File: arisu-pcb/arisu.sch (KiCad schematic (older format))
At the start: 40 parts, among them J1 USB_B_Micro, J10 PF6, J11 PF7, J12 VCC, J13 D+, J14 D-, J15 GND, J2 MISO, J3 VCC, J4 SCK, J5 MOSI, J6 RES, J7 GND, J8 PF4, J9 PF5, U1 USBLC6-2SC6, U3 AT90USB1286-MU, Y1 Crystal_GND24

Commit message: cap nhat 18:16 27/2/2021
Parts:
- removed U3: AT90USB1286-MU, Package_DFN_QFN:QFN-64-1EP_9x9mm_P0.5mm_EP7.5x7.5mm, symbol MCU_Microchip_AVR:AT90USB1286-MU
- added U2: ATmega32U4-AU, Housings_QFP:TQFP-44_10x10mm_Pitch0.8mm, symbol MCU_Microchip_ATmega:ATmega32U4-AU
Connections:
- net D+: now also U2.4 (D+)
- net D-: now also U2.3 (D-)
- net GND: now also U2.15 (GND), U2.23 (GND), U2.35 (GND), U2.43 (GND), U2.5 (UGND)
- net MISO: now also U2.11 (PB3)
- net MOSI: now also U2.10 (PB2)
- net PF4: now also U2.39 (PF4)
- net PF5: now also U2.38 (PF5)
- net PF6: now also U2.37 (PF6)
- net PF7: now also U2.36 (PF7)
- net SCK: now also U2.9 (PB1)
- net VCC: now also U2.14 (VCC), U2.2 (UVCC), U2.24 (AVCC), U2.34 (VCC), U2.44 (AVCC), U2.7 (VBUS)
- net XTAL1: now also U2.17 (XTAL1)
- net XTAL2: now also U2.16 (XTAL2)
- net col0: now also U2.41 (PF0)
- net col1: now also U2.40 (PF1)
- net col10: now also U2.29 (PB5)
- net col11: now also U2.28 (PB4)
- net col12: now also U2.27 (PD7)
- net col13: now also U2.26 (PD6)
- net col2: now also U2.1 (PE6)
- net col3: now also U2.32 (PC7)
- net col4: now also U2.31 (PC6)
- net col5: now also U2.30 (PB6)
- net col6: now also U2.25 (PD4)
- net col8: now also U2.8 (PB0)
- net col9: now also U2.12 (PB7)
- net row0: now also U2.18 (PD0)
- net row1: now also U2.19 (PD1)
- net row2: now also U2.20 (PD2)
- net row3: now also U2.21 (PD3)
- net row4: now also U2.22 (PD5)
- net ~RES~: now also U2.13 (~RESET)
- net at C4.1: now also U2.6 (UCAP)
- net at R4.1: now also U2.33 (~HWB~/PE2)
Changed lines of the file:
@@
 $EndDescr
+$Comp
+L MCU_Microchip_ATmega:ATmega32U4-AU U2
+U 1 1 5C4B1F82
+P 4500 4250
+F 0 "U2" H 4900 2400 50  0000 C CNN
+F 1 "ATmega32U4-AU" H 4900 2500 50  0000 C CNN
+F 2 "Housings_QFP:TQFP-44_10x10mm_Pitch0.8mm" H 4500 4250 50  0001 C CIN
+F 3 "http://ww1.microchip.com/downloads/en/DeviceDoc/Atmel-7766-8-bit-AVR-ATmega16U4-32U4_Datasheet.pdf" H 4500 4250 50  0001 C CNN
+	1    4500 4250
+	1    0    0    -1
+$EndComp
 $Comp
 L Connector:USB_B_Micro J1
@@
 L power:GND #PWR0116
 U 1 1 5C4F0424
-P 4475 7000
-F 0 "#PWR0116" H 4475 6750 50  0001 C CNN
-F 1 "GND" H 4480 6827 50  0000 C CNN
-F 2 "" H 4475 7000 50  0001 C CNN
-F 3 "" H 4475 7000 50  0001 C CNN
-	1    4475 7000
-	1    0    0    -1
-$EndComp
-Wire Wire Line
-	4375 6900 4375 6950
-Wire Wire Line
-	4375 6950 4475 6950
-Wire Wire Line
-	4475 6950 4475 7000
-Wire Wire Line
-	4475 6900 4475 6950
-Connection ~ 4475 6950
+P 4500 6150
+F 0 "#PWR0116" H 4500 5900 50  0001 C CNN
+F 1 "GND" H 4505 5977 50  0000 C CNN
+F 2 "" H 4500 6150 50  0001 C CNN
+F 3 "" H 4500 6150 50  0001 C CNN
+	1    4500 6150
+	1    0    0    -1
+$EndComp
+Wire Wire Line
+	4400 6050 4400 6100
+Wire Wire Line
+	4400 6100 4500 6100
+Wire Wire Line
+	4500 6100 4500 6150
+Wire Wire Line
+	4500 6050 4500 6100
+Connection ~ 4500 6100
 $Comp
 L power:VCC #PWR0117
@@
 Wire Wire Line
 	1900 4600 2750 4600
-$Comp
-L MCU_Microchip_AVR:AT90USB1286-MU U3
-U 1 1 6013B83C
-P 4500 4450
-F 0 "U3" H 4500 2361 50  0000 C CNN
-F 1 "AT90USB1286-MU" H 4500 2270 50  0000 C CNN
-F 2 "Package_DFN_QFN:QFN-64-1EP_9x9mm_P0.5mm_EP7.5x7.5mm" H 4500 4450 50  0001 C CIN
-F 3 "http://ww1.microchip.com/downloads/en/DeviceDoc/doc7593.pdf" H 4500 4450 50  0001 C CNN
-	1    4500 4450
-	1    0    0    -1
-$EndComp
 Wire Bus Line
 	5750 2700 5750 3150

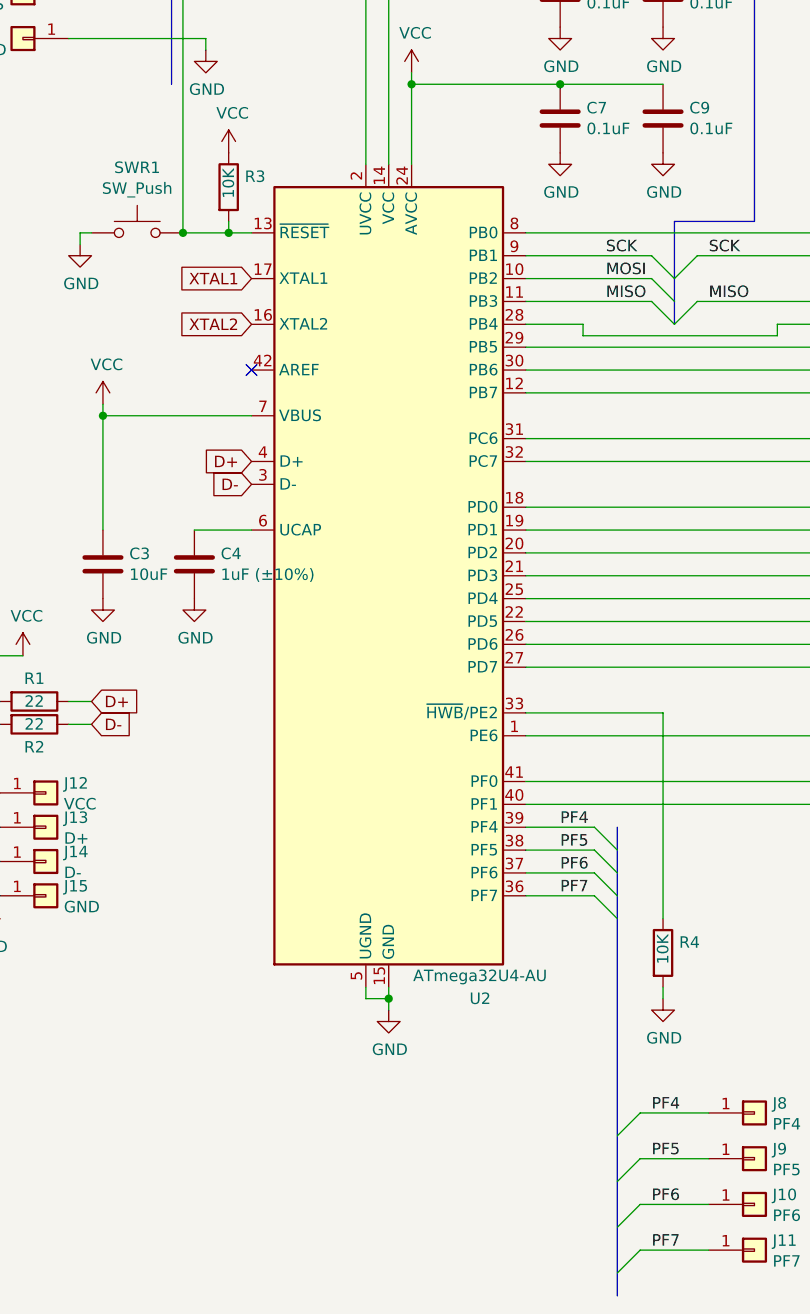
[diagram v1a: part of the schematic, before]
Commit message: add some keyboard
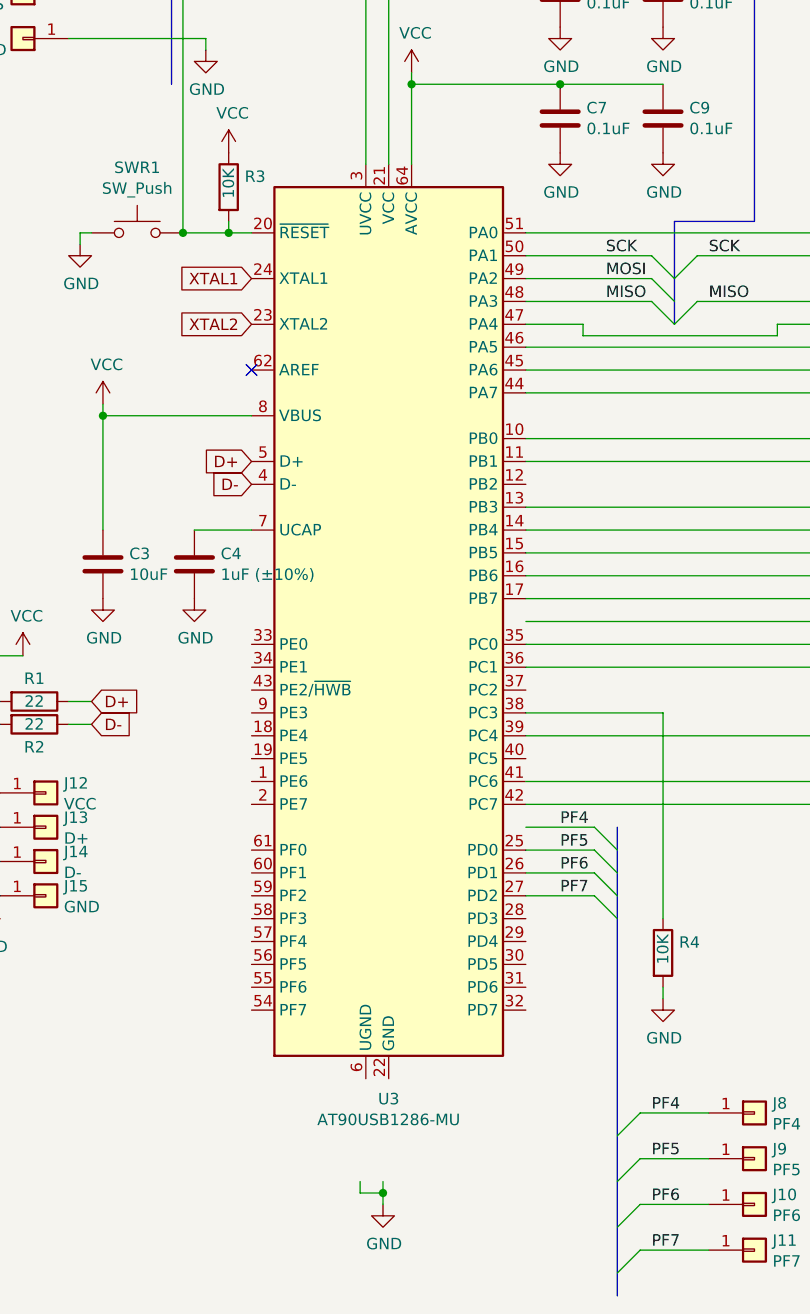
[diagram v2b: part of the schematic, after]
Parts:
- removed U2: ATmega32U4-AU, Housings_QFP:TQFP-44_10x10mm_Pitch0.8mm, symbol MCU_Microchip_ATmega:ATmega32U4-AU
- added U3: AT90USB1286-MU, Package_DFN_QFN:QFN-64-1EP_9x9mm_P0.5mm_EP7.5x7.5mm, symbol MCU_Microchip_AVR:AT90USB1286-MU
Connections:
- net D+: now also U3.5 (D+)
- net D-: now also U3.4 (D-)
- net MISO: now also U3.48 (PA3)
- net MOSI: now also U3.49 (PA2)
- net PF5: now also U3.25 (PD0)
- net PF6: now also U3.26 (PD1)
- net PF7: now also U3.27 (PD2)
- net SCK: now also U3.50 (PA1)
- net VCC: now also U3.21 (VCC), U3.3 (UVCC), U3.52 (VCC), U3.64 (AVCC), U3.8 (VBUS)
- net XTAL1: now also U3.24 (XTAL1)
- net XTAL2: now also U3.23 (XTAL2)
- net col0: now also U3.41 (PC6)
- net col1: now also U3.42 (PC7)
- net col10: now also U3.46 (PA5)
- net col11: now also U3.47 (PA4)
- net col12: now also U3.36 (PC1)
- net col13: now also U3.35 (PC0)
- net col2: now also U3.39 (PC4)
- net col3: now also U3.11 (PB1)
- net col4: now also U3.10 (PB0)
- net col5: now also U3.45 (PA6)
- net col6: now also U3.17 (PB7)
- net col8: now also U3.51 (PA0)
- net col9: now also U3.44 (PA7)
- net row0: now also U3.13 (PB3)
- net row1: now also U3.14 (PB4)
- net row2: now also U3.15 (PB5)
- net row3: now also U3.16 (PB6)
- net ~RES~: now also U3.20 (~RESET)
- net at R4.1: now also U3.38 (PC3)
- net at C4.1: now also U3.7 (UCAP)
- new net: U3.22 (GND), U3.53 (GND), U3.63 (GND), U3.65 (GND)
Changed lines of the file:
@@
 $EndDescr
-$Comp
-L MCU_Microchip_ATmega:ATmega32U4-AU U2
-U 1 1 5C4B1F82
-P 4500 4250
-F 0 "U2" H 4900 2400 50  0000 C CNN
-F 1 "ATmega32U4-AU" H 4900 2500 50  0000 C CNN
-F 2 "Housings_QFP:TQFP-44_10x10mm_Pitch0.8mm" H 4500 4250 50  0001 C CIN
-F 3 "http://ww1.microchip.com/downloads/en/DeviceDoc/Atmel-7766-8-bit-AVR-ATmega16U4-32U4_Datasheet.pdf" H 4500 4250 50  0001 C CNN
-	1    4500 4250
-	1    0    0    -1
-$EndComp
 $Comp
 L Connector:USB_B_Micro J1
@@
 L power:GND #PWR0116
 U 1 1 5C4F0424
-P 4500 6150
-F 0 "#PWR0116" H 4500 5900 50  0001 C CNN
-F 1 "GND" H 4505 5977 50  0000 C CNN
-F 2 "" H 4500 6150 50  0001 C CNN
-F 3 "" H 4500 6150 50  0001 C CNN
-	1    4500 6150
-	1    0    0    -1
-$EndComp
-Wire Wire Line
-	4400 6050 4400 6100
-Wire Wire Line
-	4400 6100 4500 6100
-Wire Wire Line
-	4500 6100 4500 6150
-Wire Wire Line
-	4500 6050 4500 6100
-Connection ~ 4500 6100
+P 4475 7000
+F 0 "#PWR0116" H 4475 6750 50  0001 C CNN
+F 1 "GND" H 4480 6827 50  0000 C CNN
+F 2 "" H 4475 7000 50  0001 C CNN
+F 3 "" H 4475 7000 50  0001 C CNN
+	1    4475 7000
+	1    0    0    -1
+$EndComp
+Wire Wire Line
+	4375 6900 4375 6950
+Wire Wire Line
+	4375 6950 4475 6950
+Wire Wire Line
+	4475 6950 4475 7000
+Wire Wire Line
+	4475 6900 4475 6950
+Connection ~ 4475 6950
 $Comp
 L power:VCC #PWR0117
@@
 Wire Wire Line
 	1900 4600 2750 4600
+$Comp
+L MCU_Microchip_AVR:AT90USB1286-MU U3
+U 1 1 6013B83C
+P 4500 4450
+F 0 "U3" H 4500 2361 50  0000 C CNN
+F 1 "AT90USB1286-MU" H 4500 2270 50  0000 C CNN
+F 2 "Package_DFN_QFN:QFN-64-1EP_9x9mm_P0.5mm_EP7.5x7.5mm" H 4500 4450 50  0001 C CIN
+F 3 "http://ww1.microchip.com/downloads/en/DeviceDoc/doc7593.pdf" H 4500 4450 50  0001 C CNN
+	1    4500 4450
+	1    0    0    -1
+$EndComp
 Wire Bus Line
 	5750 2700 5750 3150
